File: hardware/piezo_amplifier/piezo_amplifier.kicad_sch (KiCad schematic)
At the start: 14 parts, among them J1 piezo1, J2 Conn_01x04, U1 LM358

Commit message: update piezo amplifier
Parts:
- removed C1: 240pF, Capacitor_THT:C_Disc_D4.7mm_W2.5mm_P5.00mm, symbol Device:C
- removed D1: 1N4001, Diode_THT:D_DO-41_SOD81_P10.16mm_Horizontal, symbol Diode:1N4001
- removed J1: piezo1, Connector_JST:JST_XH_B2B-XH-A_1x02_P2.50mm_Vertical, symbol Connector_Generic:Conn_01x02
- removed J2: Conn_01x04, Connector_JST:JST_XH_B4B-XH-A_1x04_P2.50mm_Vertical, symbol Connector_Generic:Conn_01x04
- removed R1: 1M, Resistor_THT:R_Axial_DIN0204_L3.6mm_D1.6mm_P5.08mm_Vertical, symbol Device:R_Small
- removed R2, R3: 1k, Resistor_THT:R_Axial_DIN0204_L3.6mm_D1.6mm_P5.08mm_Vertical, symbol Device:R_Small
- removed R4: 220k, Resistor_THT:R_Axial_DIN0204_L3.6mm_D1.6mm_P5.08mm_Vertical, symbol Device:R_Small
- removed RV1: 2MOhm, Connector_JST:JST_XH_B3B-XH-A_1x03_P2.50mm_Vertical, symbol Device:R_POT
- removed U1: LM358, Package_DIP:DIP-8_W7.62mm_LongPads, symbol Amplifier_Operational:LM358
- added C? (x2): 680pF, symbol Device:C
- added P? (x3): Conn_01x02, Connector_JST:JST_XH_B2B-XH-A_1x02_P2.50mm_Vertical, symbol Connector_Generic:Conn_01x02
- added R? (x5): 10k, symbol Device:R_Small
- added R? (x2): 270M, symbol Device:R_Small
- added R?: 3k, symbol Device:R_Small
- added R?: 20k, symbol Device:R_Small
- added RV?: R_Potentiometer, symbol Device:R_Potentiometer
- added U? (x5): Opamp_Quad, symbol Device:Opamp_Quad
- added U? (x3): LM393, symbol Comparator:LM393
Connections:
- net GND: now also P?.2 (Pin_2), P?.2 (Pin_2), R?.2, RV?.3, U?.11 (V-), U?.4 (V-)
- new net: P?.1 (Pin_1), R?.1
- new net: P?.2 (Pin_2), R?.1
- new net: C?.1, R?.1, R?.2, U?.3 (+)
- new net: C?.2, R?.1, R?.2, U?.1
- new net: R?.1, R?.2, U?.6 (-)
- new net: R?.1, U?.1
- new net: RV?.2, U?.2 (-)
- new net: R?.2, U?.3 (+), U?.7
- new net: C?.1, R?.1, R?.2, U?.2 (-)
- new net +12V: P?.1 (Pin_1), P?.1 (Pin_1), R?.1, R?.2, RV?.1, U?.8 (V+)
- new net +6V: C?.2, R?.1, R?.2, R?.2, U?.5 (+)
- no-connect marks 2 -> 0
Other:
- note added: "Based on the design published here https://www.ti.com/lit/an/slyt369/slyt369.pdf?ts=1659992224665"

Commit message: update piezo amplifier board
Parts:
- removed R? (x2): 10k, symbol Device:R_Small
- added U?: (no value), symbol Regulator_Linear:L7806
- C? (x2): value 680pF -> (none)
- R? (x2): value 270M -> (none)
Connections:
- net +12V: now also U?.1 (IN)
- net +6V: now also U?.3 (OUT)
- net GND: now also U?.2 (GND)

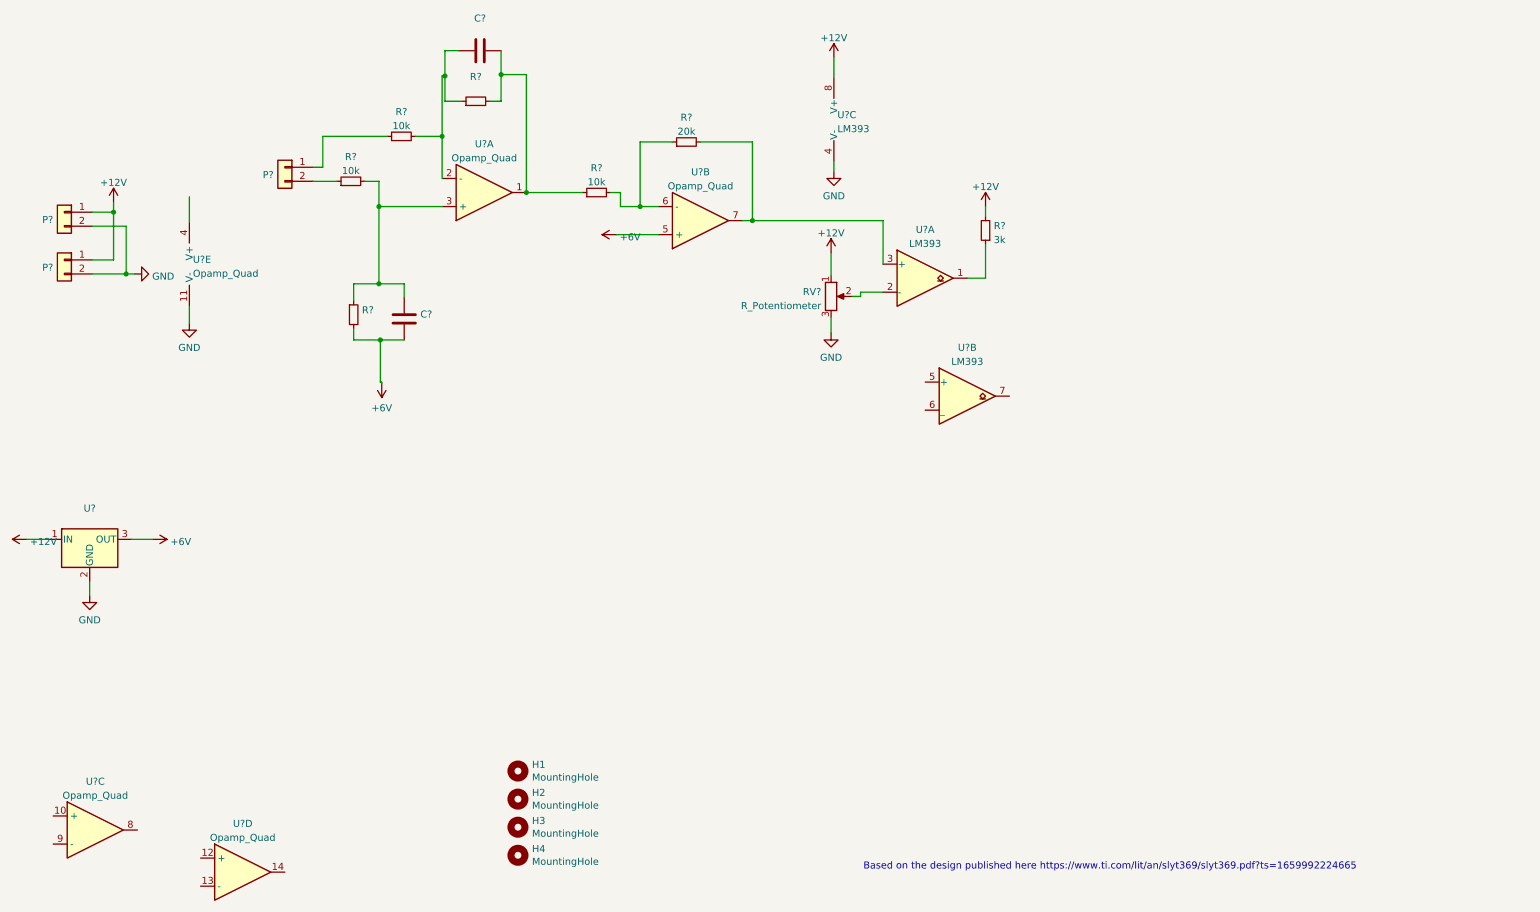
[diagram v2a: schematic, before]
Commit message: update piezo amplfier
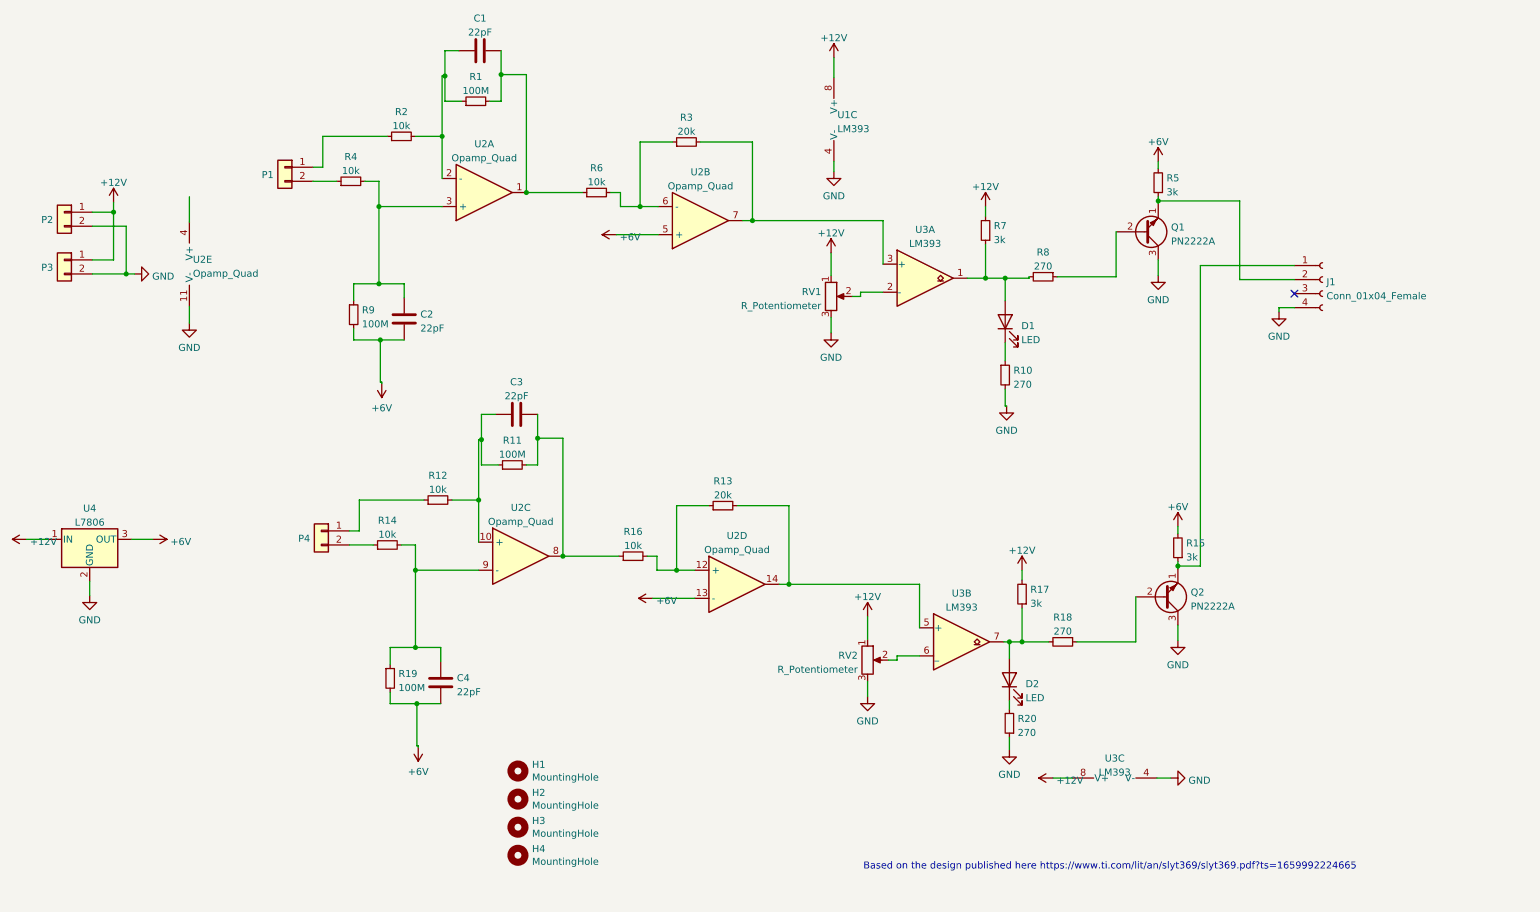
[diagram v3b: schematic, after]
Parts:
- removed U? (x2): LM393, symbol Comparator:LM393
- added C3, C4: 22pF, Capacitor_THT:C_Disc_D16.0mm_W5.0mm_P10.00mm, symbol Device:C
- added D1, D2: LED, LED_THT:LED_D3.0mm_Clear, symbol Device:LED
- added J1: Conn_01x04_Female, Connector_JST:JST_XH_B4B-XH-A_1x04_P2.50mm_Vertical, symbol Connector:Conn_01x04_Female
- added P4: Conn_01x02, Connector_JST:JST_XH_B2B-XH-A_1x02_P2.50mm_Vertical, symbol Connector_Generic:Conn_01x02
- added Q1, Q2: PN2222A, Package_TO_SOT_THT:TO-92_Inline, symbol Transistor_BJT:PN2222A
- added R10, R18, R20, R8: 270, Resistor_THT:R_Axial_DIN0411_L9.9mm_D3.6mm_P15.24mm_Horizontal, symbol Device:R_Small
- added R11, R19: 100M, Resistor_THT:R_Axial_DIN0411_L9.9mm_D3.6mm_P15.24mm_Horizontal, symbol Device:R_Small
- added R12, R14, R16: 10k, Resistor_THT:R_Axial_DIN0411_L9.9mm_D3.6mm_P15.24mm_Horizontal, symbol Device:R_Small
- added R13: 20k, Resistor_THT:R_Axial_DIN0411_L9.9mm_D3.6mm_P15.24mm_Horizontal, symbol Device:R_Small
- added R15, R17, R5: 3k, Resistor_THT:R_Axial_DIN0411_L9.9mm_D3.6mm_P15.24mm_Horizontal, symbol Device:R_Small
- added RV2: R_Potentiometer, Connector_JST:JST_XH_B3B-XH-A_1x03_P2.50mm_Vertical, symbol Device:R_Potentiometer
- added U3: LM393, Package_DIP:DIP-8_W7.62mm_Socket_LongPads, symbol Comparator:LM393
- C1, C2: renamed from C?; value (none) -> 22pF; footprint (none) -> Capacitor_THT:C_Disc_D16.0mm_W5.0mm_P10.00mm
- R1, R9: renamed from R?; value (none) -> 100M; footprint (none) -> Resistor_THT:R_Axial_DIN0411_L9.9mm_D3.6mm_P15.24mm_Horizontal
- R2, R3, R4, R6, R7: renamed from R?; footprint (none) -> Resistor_THT:R_Axial_DIN0411_L9.9mm_D3.6mm_P15.24mm_Horizontal
- RV1: renamed from RV?; footprint (none) -> Connector_JST:JST_XH_B3B-XH-A_1x03_P2.50mm_Vertical
- U1: renamed from U?; footprint (none) -> Package_DIP:DIP-8_W7.62mm_Socket_LongPads
- U2: renamed from U?; footprint (none) -> Package_DIP:DIP-14_W7.62mm_Socket_LongPads
- U4: renamed from U?; value (none) -> L7806; footprint (none) -> Package_TO_SOT_THT:TO-3P-3_Vertical
- gave numbers to parts that had none: 3
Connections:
- net +12V: now also R17.2, RV2.1, U3.8 (V+)
- net +6V: now also U2.13 (-), C4.2, R15.2, R19.2, R5.2
- net GND: now also J1.4 (Pin_4), Q1.3 (C), Q2.3 (C), R10.2, R20.1, RV2.3, U3.4 (V-)
- net at R7.1: now also D1.2 (A), R8.2, U3.1
- net at RV1.2: now also U3.2 (-)
- net at R3.2, U2.7: now also U3.3 (+)
- net at U2.12 (+): now also R13.1, R16.2
- net at U2.14: now also R13.2, U3.5 (+)
- net at U2.10 (+): now also C3.1, R11.1, R12.2
- net at U2.8: now also C3.2, R11.2, R16.1
- net at U2.9 (-): now also C4.1, R14.2, R19.1
- new net: P4.1 (Pin_1), R12.1
- new net: P4.2 (Pin_2), R14.1
- new net: D2.1 (K), R20.2
- new net: J1.1 (Pin_1), Q2.1 (E), R15.1
- new net: J1.2 (Pin_2), Q1.1 (E), R5.1
- new net: D1.1 (K), R10.1
- new net: RV2.2, U3.6 (_)
- new net: Q1.2 (B), R8.1
- new net: Q2.2 (B), R18.1
- new net: D2.2 (A), R17.1, R18.2, U3.7
- no-connect marks 0 -> 1
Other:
- moved on the sheet: U2C, U2D
